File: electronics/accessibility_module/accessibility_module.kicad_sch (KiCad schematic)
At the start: 9 parts, among them M1 Motor_DC, M2 Motor_Servo, M3 Motor_Servo, M4 Motor_Servo, M5 Motor_Servo, Q1 BC546, U1 ESP32-C3-DevKitM-1

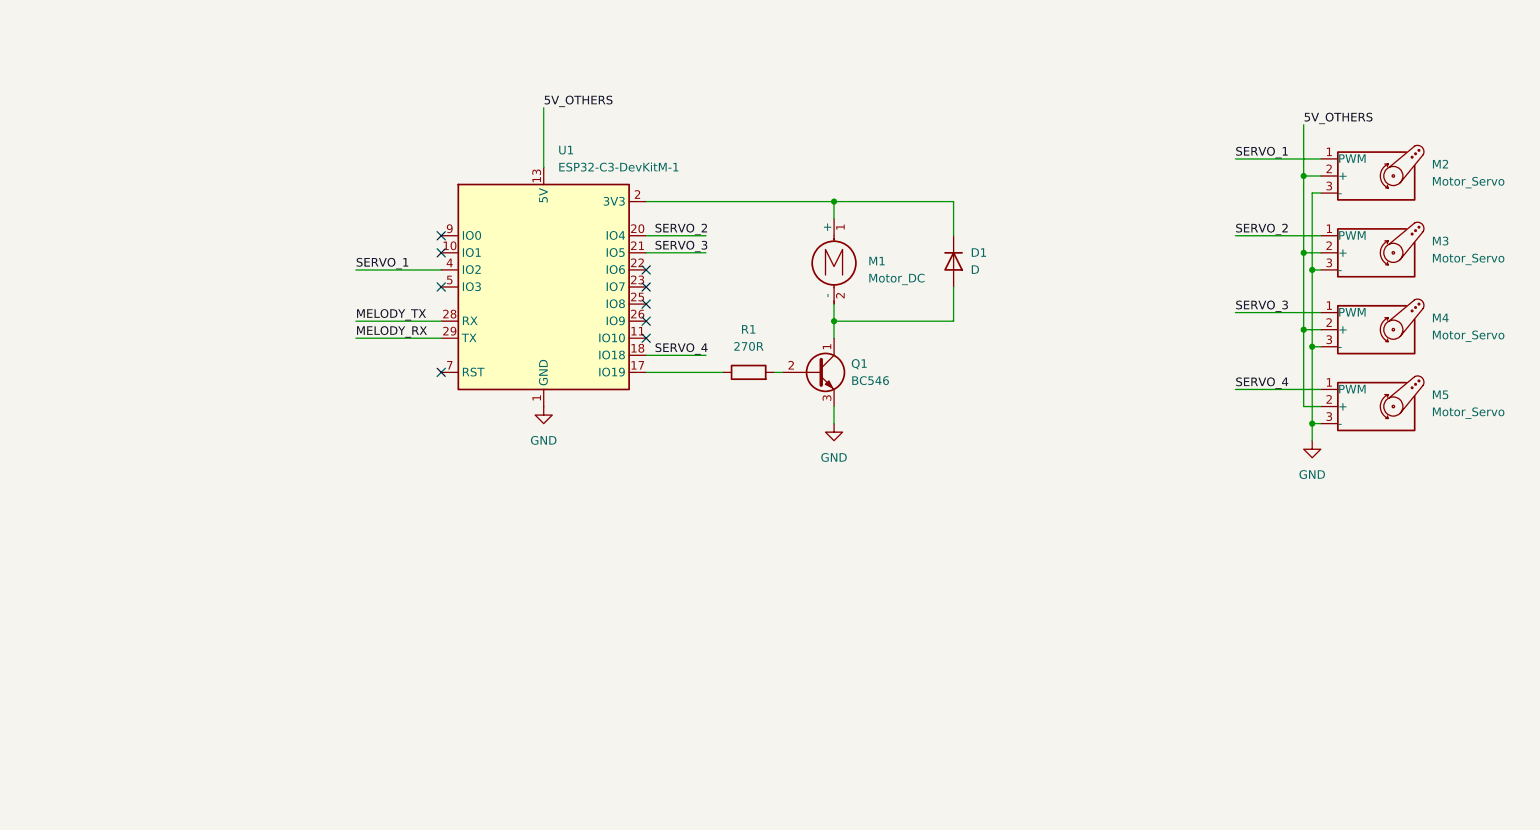
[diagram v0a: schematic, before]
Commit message: change IC 74->40 + shared power supply for processors + PCB
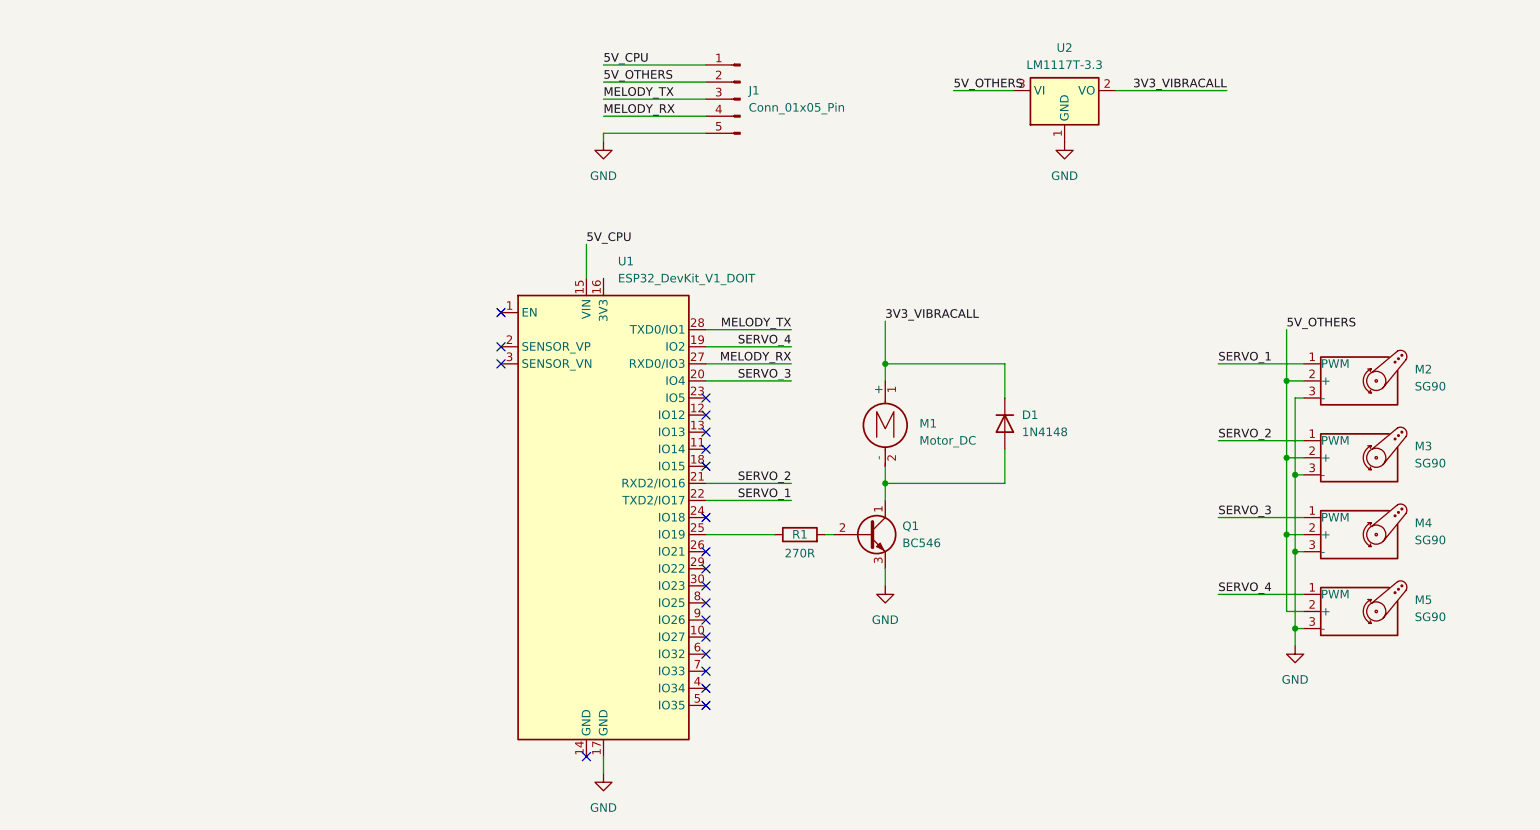
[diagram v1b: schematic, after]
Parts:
- removed U1: ESP32-C3-DevKitM-1, RF_Module:ESP32-C3-DevKitM-1, symbol RF_Module:ESP32-C3-DevKitM-1
- added J1: Conn_01x05_Pin, Connector_PinHeader_2.54mm:PinHeader_1x05_P2.54mm_Vertical, symbol Connector:Conn_01x05_Pin
- added U1: ESP32_DevKit_V1_DOIT, esp32_devkit_v1_doit:esp32_devkit_v1_doit, symbol esp32_devkit_v1_doit:ESP32_DevKit_V1_DOIT
- added U2: LM1117T-3.3, Package_TO_SOT_THT:TO-220-3_Vertical, symbol Regulator_Linear:LM1117T-3.3
- D1: value D -> 1N4148; footprint (none) -> Diode_THT:D_DO-35_SOD27_P7.62mm_Horizontal
- M1: footprint (none) -> Connector_PinHeader_2.54mm:PinHeader_1x02_P2.54mm_Vertical
- M2, M3, M4, M5: value Motor_Servo -> SG90; footprint (none) -> Connector_PinHeader_2.54mm:PinHeader_1x03_P2.54mm_Vertical
- R1: footprint (none) -> Resistor_THT:R_Axial_DIN0204_L3.6mm_D1.6mm_P7.62mm_Horizontal
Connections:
- net 5V_OTHERS: now also J1.2 (Pin_2), U2.3 (VI)
- net GND: now also J1.5 (Pin_5), U1.17 (GND), U2.1 (GND)
- net MELODY_RX: now also J1.4 (Pin_4), U1.27 (RXD0/IO3)
- net MELODY_TX: now also J1.3 (Pin_3), U1.28 (TXD0/IO1)
- net SERVO_1: now also U1.22 (TXD2/IO17)
- net SERVO_2: now also U1.21 (RXD2/IO16)
- net SERVO_3: now also U1.20 (IO4)
- net SERVO_4: now also U1.19 (IO2)
- net at R1.1: now also U1.25 (IO19)
- net 3V3_VIBRACALL: now reaches D1.1 (K), M1.1 (+)
- net 3V3_VIBRACALL: now also U2.2 (VO)
- new net 5V_CPU: J1.1 (Pin_1), U1.15 (VIN)
- no-connect marks 9 -> 20
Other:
- company: (none) -> UTFPR
- title: (none) -> Accessibility Module
- moved on the sheet: D1, M1, M2, M3, M4, M5, Q1, R1

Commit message: Atualização esquemático eletrônico
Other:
- moved on the sheet: D1, J1, M1, Q1, R1, U2
